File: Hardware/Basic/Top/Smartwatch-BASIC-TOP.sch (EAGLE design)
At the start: 60 parts, among them SW6 SWITCH.MOM, SW7 SWITCH.MOM, U2 NRF52832_MODULE_MDBT42, U4 FT231XS

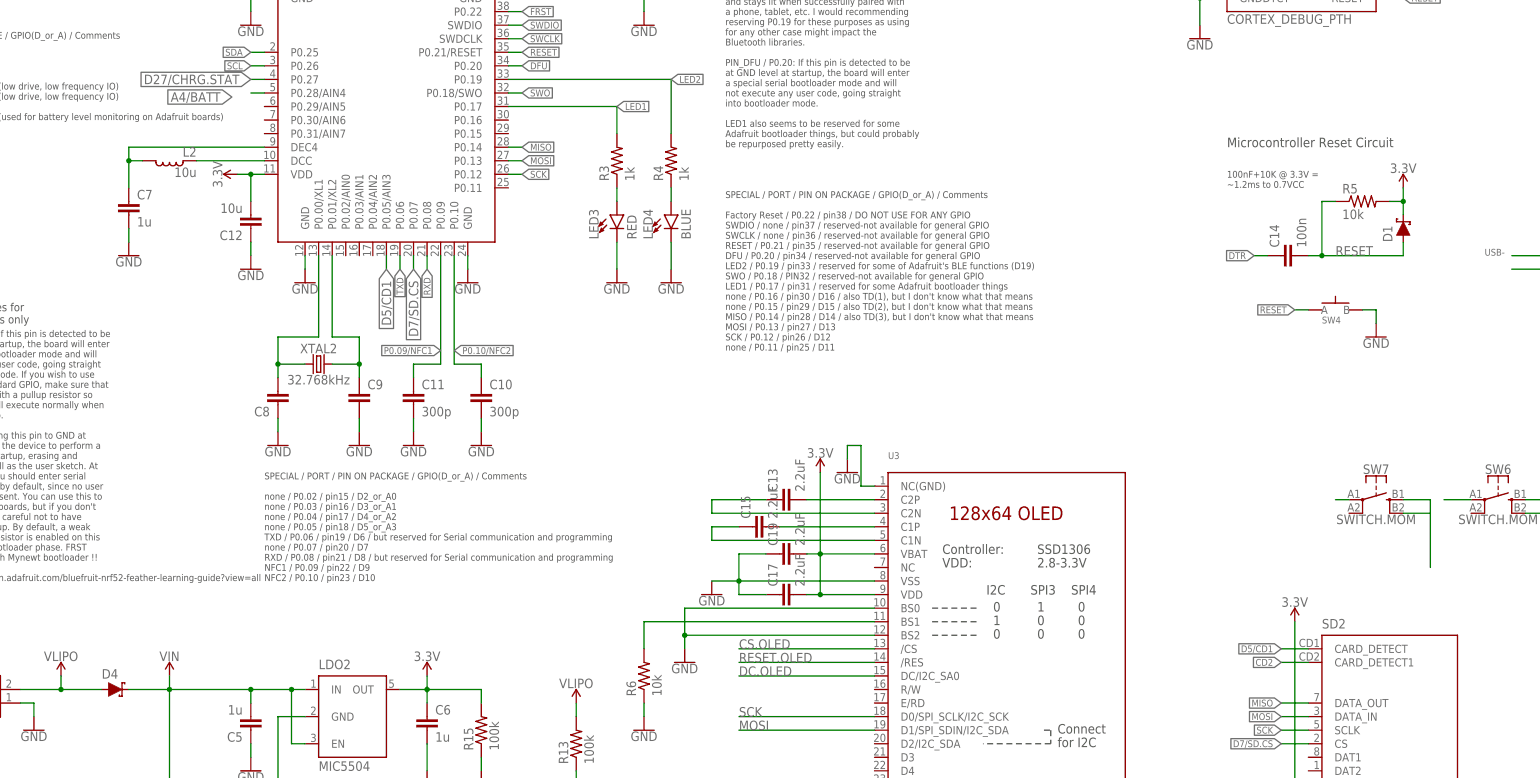
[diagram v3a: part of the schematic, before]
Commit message: Bottom board routed
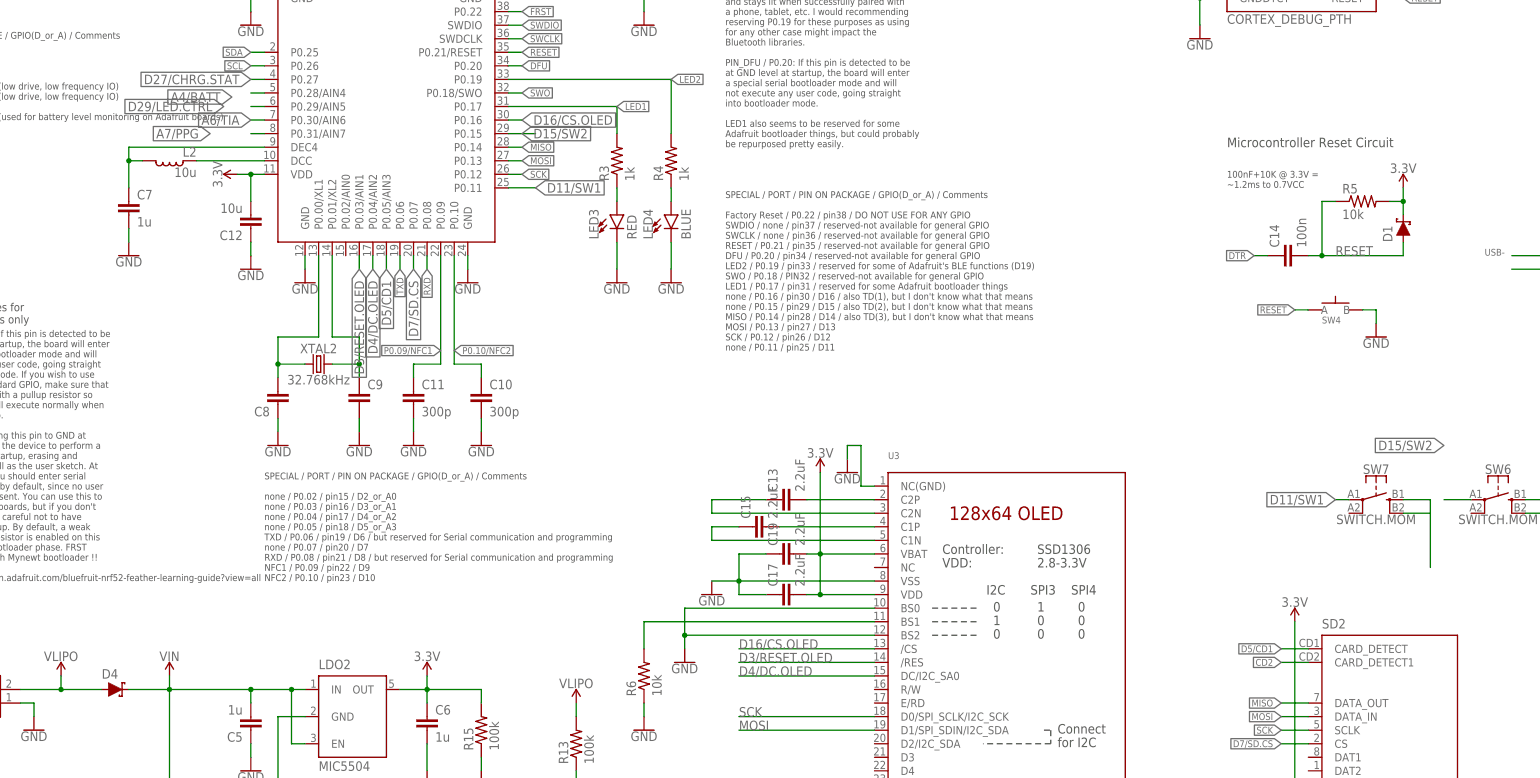
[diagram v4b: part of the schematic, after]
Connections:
- removed net CS.OLED: U3./CS
- removed net DC.OLED: U3.DC/I2C_SA0
- removed net N$23: SW6.1
- removed net N$24: SW7.1
- removed net RESET.OLED: U3./RES
- new net A6/TIA: U2.P0.30/AIN6
- new net A7/PPG: U2.P0.31/AIN7
- new net D11/SW1: SW7.1, U2.P0.11
- new net D15/SW2: SW6.1, U2.P0.15
- new net D16/CS.OLED: U2.P0.16, U3./CS
- new net D29/LED.CTRL: U2.P0.29/AIN5
- new net D3/RESET.OLED: U2.P0.03/AIN1, U3./RES
- new net D4/DC.OLED: U2.P0.04/AIN2, U3.DC/I2C_SA0
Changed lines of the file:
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@@
 </segment>
 </net>
-<net name="DC.OLED" class="0">
+<net name="D4/DC.OLED" class="0">
 <segment>
 <label x="154.94" y="-10.16" size="1.778" layer="95"/>
@@
 <wire x1="180.34" y1="-10.16" x2="154.94" y2="-10.16" width="0.1524" layer="91"/>
 </segment>
-</net>
-<net name="RESET.OLED" class="0">
-<segment>
-<label x="154.94" y="-7.62" size="1.778" layer="95"/>
-<pinref part="U3" gate="G$1" pin="/RES"/>
-<wire x1="180.34" y1="-7.62" x2="154.94" y2="-7.62" width="0.1524" layer="91"/>
+<segment>
+<pinref part="U2" gate="G$1" pin="P0.04/AIN2"/>
+<wire x1="86.36" y1="68.58" x2="86.36" y2="66.04" width="0.1524" layer="91"/>
+<label x="86.36" y="66.04" size="1.778" layer="95" rot="R270" xref="yes"/>
 </segment>
 </net>
@@
 </segment>
 </net>
-<net name="CS.OLED" class="0">
+<net name="D16/CS.OLED" class="0">
 <segment>
 <label x="154.94" y="-5.08" size="1.778" layer="95"/>
 <pinref part="U3" gate="G$1" pin="/CS"/>
 <wire x1="180.34" y1="-5.08" x2="154.94" y2="-5.08" width="0.1524" layer="91"/>
+</segment>
+<segment>
+<pinref part="U2" gate="G$1" pin="P0.16"/>
+<wire x1="111.76" y1="93.98" x2="114.3" y2="93.98" width="0.1524" layer="91"/>
+<label x="114.3" y="93.98" size="1.778" layer="95" xref="yes"/>
 </segment>
 </net>
@@
 </segment>
 </net>
-<net name="N$23" class="0">
-<segment>
-<pinref part="SW6" gate="G$1" pin="1"/>
-<wire x1="292.1" y1="22.86" x2="287.02" y2="22.86" width="0.1524" layer="91"/>
-</segment>
-</net>
-<net name="N$24" class="0">
-<segment>
-<pinref part="SW7" gate="G$1" pin="1"/>
-<wire x1="269.24" y1="22.86" x2="266.7" y2="22.86" width="0.1524" layer="91"/>
-</segment>
-</net>
 <net name="CD2" class="0">
 <segment>
@@
 </segment>
 </net>
+<net name="D11/SW1" class="0">
+<segment>
+<pinref part="U2" gate="G$1" pin="P0.11"/>
+<wire x1="111.76" y1="81.28" x2="116.84" y2="81.28" width="0.1524" layer="91"/>
+<label x="116.84" y="81.28" size="1.778" layer="95" xref="yes"/>
+</segment>
+<segment>
+<pinref part="SW7" gate="G$1" pin="1"/>
+<wire x1="269.24" y1="22.86" x2="266.7" y2="22.86" width="0.1524" layer="91"/>
+<label x="266.7" y="22.86" size="1.778" layer="95" rot="R180" xref="yes"/>
+</segment>
+</net>
+<net name="D15/SW2" class="0">
+<segment>
+<pinref part="U2" gate="G$1" pin="P0.15"/>
+<wire x1="111.76" y1="91.44" x2="116.84" y2="91.44" width="0.1524" layer="91"/>
+<label x="114.3" y="91.44" size="1.778" layer="95" xref="yes"/>
+</segment>
+<segment>
+<pinref part="SW6" gate="G$1" pin="1"/>
+<wire x1="292.1" y1="22.86" x2="287.02" y2="22.86" width="0.1524" layer="91"/>
+<label x="287.02" y="33.02" size="1.778" layer="95" rot="R180" xref="yes"/>
+</segment>
+</net>
+<net name="D3/RESET.OLED" class="0">
+<segment>
+<pinref part="U2" gate="G$1" pin="P0.03/AIN1"/>
+<wire x1="83.82" y1="68.58" x2="83.82" y2="66.04" width="0.1524" layer="91"/>
+<label x="83.82" y="66.04" size="1.778" layer="95" rot="R270" xref="yes"/>
+</segment>
+<segment>
+<label x="154.94" y="-7.62" size="1.778" layer="95"/>
+<pinref part="U3" gate="G$1" pin="/RES"/>
+<wire x1="180.34" y1="-7.62" x2="154.94" y2="-7.62" width="0.1524" layer="91"/>
+</segment>
+</net>
+<net name="D29/LED.CTRL" class="0">
+<segment>
+<pinref part="U2" gate="G$1" pin="P0.29/AIN5"/>
+<wire x1="66.04" y1="96.52" x2="63.5" y2="96.52" width="0.1524" layer="91"/>
+<label x="58.42" y="96.52" size="1.778" layer="95" rot="R180" xref="yes"/>
+</segment>
+</net>
+<net name="A6/TIA" class="0">
+<segment>
+<pinref part="U2" gate="G$1" pin="P0.30/AIN6"/>
+<wire x1="66.04" y1="93.98" x2="63.5" y2="93.98" width="0.1524" layer="91"/>
+<label x="63.5" y="93.98" size="1.778" layer="95" rot="R180" xref="yes"/>
+</segment>
+</net>
+<net name="A7/PPG" class="0">
+<segment>
+<pinref part="U2" gate="G$1" pin="P0.31/AIN7"/>
+<wire x1="66.04" y1="91.44" x2="63.5" y2="91.44" width="0.1524" layer="91"/>
+<label x="55.88" y="91.44" size="1.778" layer="95" rot="R180" xref="yes"/>
+</segment>
+</net>

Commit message: Top Board Routed
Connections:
- net 3.3V: now also J1.4
- net A6/TIA: now also J1.5
- net A7/PPG: now also J1.7
- net D29/LED.CTRL: now also J1.6
- net GND: now also J1.3
- net SCL: now also J1.2
- net SDA: now also J1.1
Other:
- moved on the sheet: J1
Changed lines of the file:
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@@
 <part name="SUPPLY1" library="LinnesLab-Symbols" deviceset="3.3V" device=""/>
 <part name="SUPPLY7" library="LinnesLab-Symbols" deviceset="3.3V" device=""/>
+<part name="SUPPLY8" library="LinnesLab-Symbols" deviceset="3.3V" device=""/>
+<part name="GND1" library="LinnesLab-Symbols" deviceset="GND" device=""/>
 </parts>
 <sheets>
@@
 <attribute name="VALUE" x="274.32" y="20.066" size="1.778" layer="96" font="vector" align="top-center"/>
 </instance>
-<instance part="J1" gate="G$1" x="-15.24" y="40.64" smashed="yes">
-<attribute name="VALUE" x="-20.32" y="30.734" size="1.778" layer="96" font="vector"/>
-<attribute name="NAME" x="-20.32" y="53.848" size="1.778" layer="95" font="vector"/>
+<instance part="J1" gate="G$1" x="-30.48" y="33.02" smashed="yes">
+<attribute name="VALUE" x="-35.56" y="23.114" size="1.778" layer="96" font="vector"/>
+<attribute name="NAME" x="-35.56" y="46.228" size="1.778" layer="95" font="vector"/>
 </instance>
 <instance part="SUPPLY6" gate="G$1" x="259.08" y="0" smashed="yes">
@@
 <instance part="SUPPLY7" gate="G$1" x="10.16" y="142.24" smashed="yes">
 <attribute name="VALUE" x="10.16" y="145.034" size="1.778" layer="96" align="bottom-center"/>
+</instance>
+<instance part="SUPPLY8" gate="G$1" x="-22.86" y="53.34" smashed="yes">
+<attribute name="VALUE" x="-22.86" y="56.134" size="1.778" layer="96" align="bottom-center"/>
+</instance>
+<instance part="GND1" gate="G$1" x="-22.86" y="17.78" smashed="yes">
+<attribute name="VALUE" x="-22.86" y="17.526" size="1.778" layer="96" align="top-center"/>
 </instance>
 </instances>
@@
 <wire x1="320.04" y1="53.34" x2="320.04" y2="50.8" width="0.1524" layer="91"/>
 </segment>
+<segment>
+<pinref part="J1" gate="G$1" pin="3"/>
+<wire x1="-25.4" y1="33.02" x2="-22.86" y2="33.02" width="0.1524" layer="91"/>
+<wire x1="-22.86" y1="33.02" x2="-22.86" y2="20.32" width="0.1524" layer="91"/>
+<pinref part="GND1" gate="G$1" pin="GND"/>
+</segment>
 </net>
 <net name="SWDIO" class="0">
@@
 <pinref part="SUPPLY7" gate="G$1" pin="3.3V"/>
 </segment>
+<segment>
+<pinref part="J1" gate="G$1" pin="4"/>
+<wire x1="-25.4" y1="35.56" x2="-22.86" y2="35.56" width="0.1524" layer="91"/>
+<wire x1="-22.86" y1="35.56" x2="-22.86" y2="53.34" width="0.1524" layer="91"/>
+<pinref part="SUPPLY8" gate="G$1" pin="3.3V"/>
+</segment>
 </net>
 <net name="SDA" class="0">
@@
 <label x="-5.08" y="124.46" size="1.778" layer="95" rot="R180" xref="yes"/>
 </segment>
+<segment>
+<pinref part="J1" gate="G$1" pin="1"/>
+<wire x1="-25.4" y1="27.94" x2="-22.86" y2="27.94" width="0.1524" layer="91"/>
+<label x="-22.86" y="27.94" size="1.778" layer="95" xref="yes"/>
+</segment>
 </net>
 <net name="SCL" class="0">
@@
 <wire x1="10.16" y1="124.46" x2="20.32" y2="124.46" width="0.1524" layer="91"/>
 <label x="20.32" y="124.46" size="1.778" layer="95" xref="yes"/>
+</segment>
+<segment>
+<pinref part="J1" gate="G$1" pin="2"/>
+<wire x1="-25.4" y1="30.48" x2="-22.86" y2="30.48" width="0.1524" layer="91"/>
+<label x="-22.86" y="30.48" size="1.778" layer="95" xref="yes"/>
 </segment>
 </net>
@@
 <label x="58.42" y="96.52" size="1.778" layer="95" rot="R180" xref="yes"/>
 </segment>
+<segment>
+<pinref part="J1" gate="G$1" pin="6"/>
+<wire x1="-25.4" y1="40.64" x2="-22.86" y2="40.64" width="0.1524" layer="91"/>
+<label x="-22.86" y="40.64" size="1.778" layer="95" xref="yes"/>
+</segment>
 </net>
 <net name="A6/TIA" class="0">
@@
 <label x="63.5" y="93.98" size="1.778" layer="95" rot="R180" xref="yes"/>
 </segment>
+<segment>
+<pinref part="J1" gate="G$1" pin="5"/>
+<wire x1="-25.4" y1="38.1" x2="-22.86" y2="38.1" width="0.1524" layer="91"/>
+<label x="-22.86" y="38.1" size="1.778" layer="95" xref="yes"/>
+</segment>
 </net>
 <net name="A7/PPG" class="0">
@@
 <label x="55.88" y="91.44" size="1.778" layer="95" rot="R180" xref="yes"/>
 </segment>
-</net>
+<segment>
+<pinref part="J1" gate="G$1" pin="7"/>
+<wire x1="-25.4" y1="43.18" x2="-22.86" y2="43.18" width="0.1524" layer="91"/>
+<label x="-22.86" y="43.18" size="1.778" layer="95" xref="yes"/>
+</segment>
+</net>

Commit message: Top Board Routed
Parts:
- removed C20, C21: 4.7u, LinnesLab-Passives:CAPACITOR0603
- removed C5, C6: 1u, LinnesLab-Passives:CAPACITOR0603
- removed CHRG2: MCP73831, LinnesLab-Power:MCP73831
- removed LDO2: MIC5504, LinnesLab-Power:MIC5504
- removed R11: (no value), LinnesLab-Passives:RESISTOR0603
- removed R12, R15: 100k, LinnesLab-Passives:RESISTOR0603
- removed SD2: (no value), LinnesLab-Connectors:MICROSD
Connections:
- removed net CD2: SD2.CARD_DETECT1
- removed net N$17: CHRG2.PROG, R11.2
- net 3.3V: no longer C6.1, LDO2.OUT, R15.2, SD2.VDD
- net D27/CHRG.STAT: no longer CHRG2.STAT, R12.1
- net D5/CD1: no longer SD2.CARD_DETECT
- net D7/SD.CS: no longer SD2.CS
- net GND: no longer C20.2, C21.1, C5.1, C6.2, CHRG2.VSS, LDO2.GND, R11.1, R15.1, SD2.GND, SD2.GND1, SD2.VSS
- net MISO: no longer SD2.DATA_OUT
- net MOSI: no longer SD2.DATA_IN
- net SCK: no longer SD2.SCLK
- net VIN: no longer C21.2, C5.2, CHRG2.VIN, LDO2.EN, LDO2.IN, R12.2
- net VLIPO: no longer C20.1, CHRG2.VBAT
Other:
- note removed: "Connect MISO, MOSI, and SCK to appropriate pins on microcontroller. Those are SPI pins and are generally prespecified. You have more flexibility with the SD.CS pin."

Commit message: Rearranged Top Board
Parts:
- added C1, C3: 4.7u, LinnesLab-Passives:CAPACITOR0603
- added C5, C6: 1u, LinnesLab-Passives:CAPACITOR0603
- added CHRG2: MCP73831, LinnesLab-Power:MCP73831
- added LDO2: MIC5504, LinnesLab-Power:MIC5504
- added R11: (no value), LinnesLab-Passives:RESISTOR0603
- added R12, R8: 100k, LinnesLab-Passives:RESISTOR0603
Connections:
- new net N$16: CHRG2.PROG, R11.2
- new net VIN1: C1.2, C5.2, CHRG2.VIN, LDO2.EN, LDO2.IN, R12.2
- net 3.3V: now also C6.1, LDO2.OUT, R8.2
- net D27/CHRG.STAT: now also CHRG2.STAT, R12.1
- net GND: now also C1.1, C3.2, C5.1, C6.2, CHRG2.VSS, LDO2.GND, R11.1, R8.1
- net VLIPO: now also C3.1, CHRG2.VBAT

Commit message: Organized Schematics and Silkscreens for both boards
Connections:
- removed net VIN1: C1.2, C5.2, CHRG2.VIN, LDO2.EN, LDO2.IN, R12.2
- net VIN: now also C1.2, C5.2, CHRG2.VIN, LDO2.EN, LDO2.IN, R12.2
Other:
- note added: "Buttons"
- note added: "Cortex Debugger/ Programmer"
- note added: "FTDI"
- note added: "Header Pins"
- note added: "Power Management"
- note added: "nRF2832"
- moved on the sheet: C1, C10, C11, C12, C13, C14, C15, C16, C17, C18, C19, C22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
